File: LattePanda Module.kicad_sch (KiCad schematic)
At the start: 12 parts, among them CN78 SMTWE2055MTJ, CN79 SMTWE2055MTJ, J81 I2C

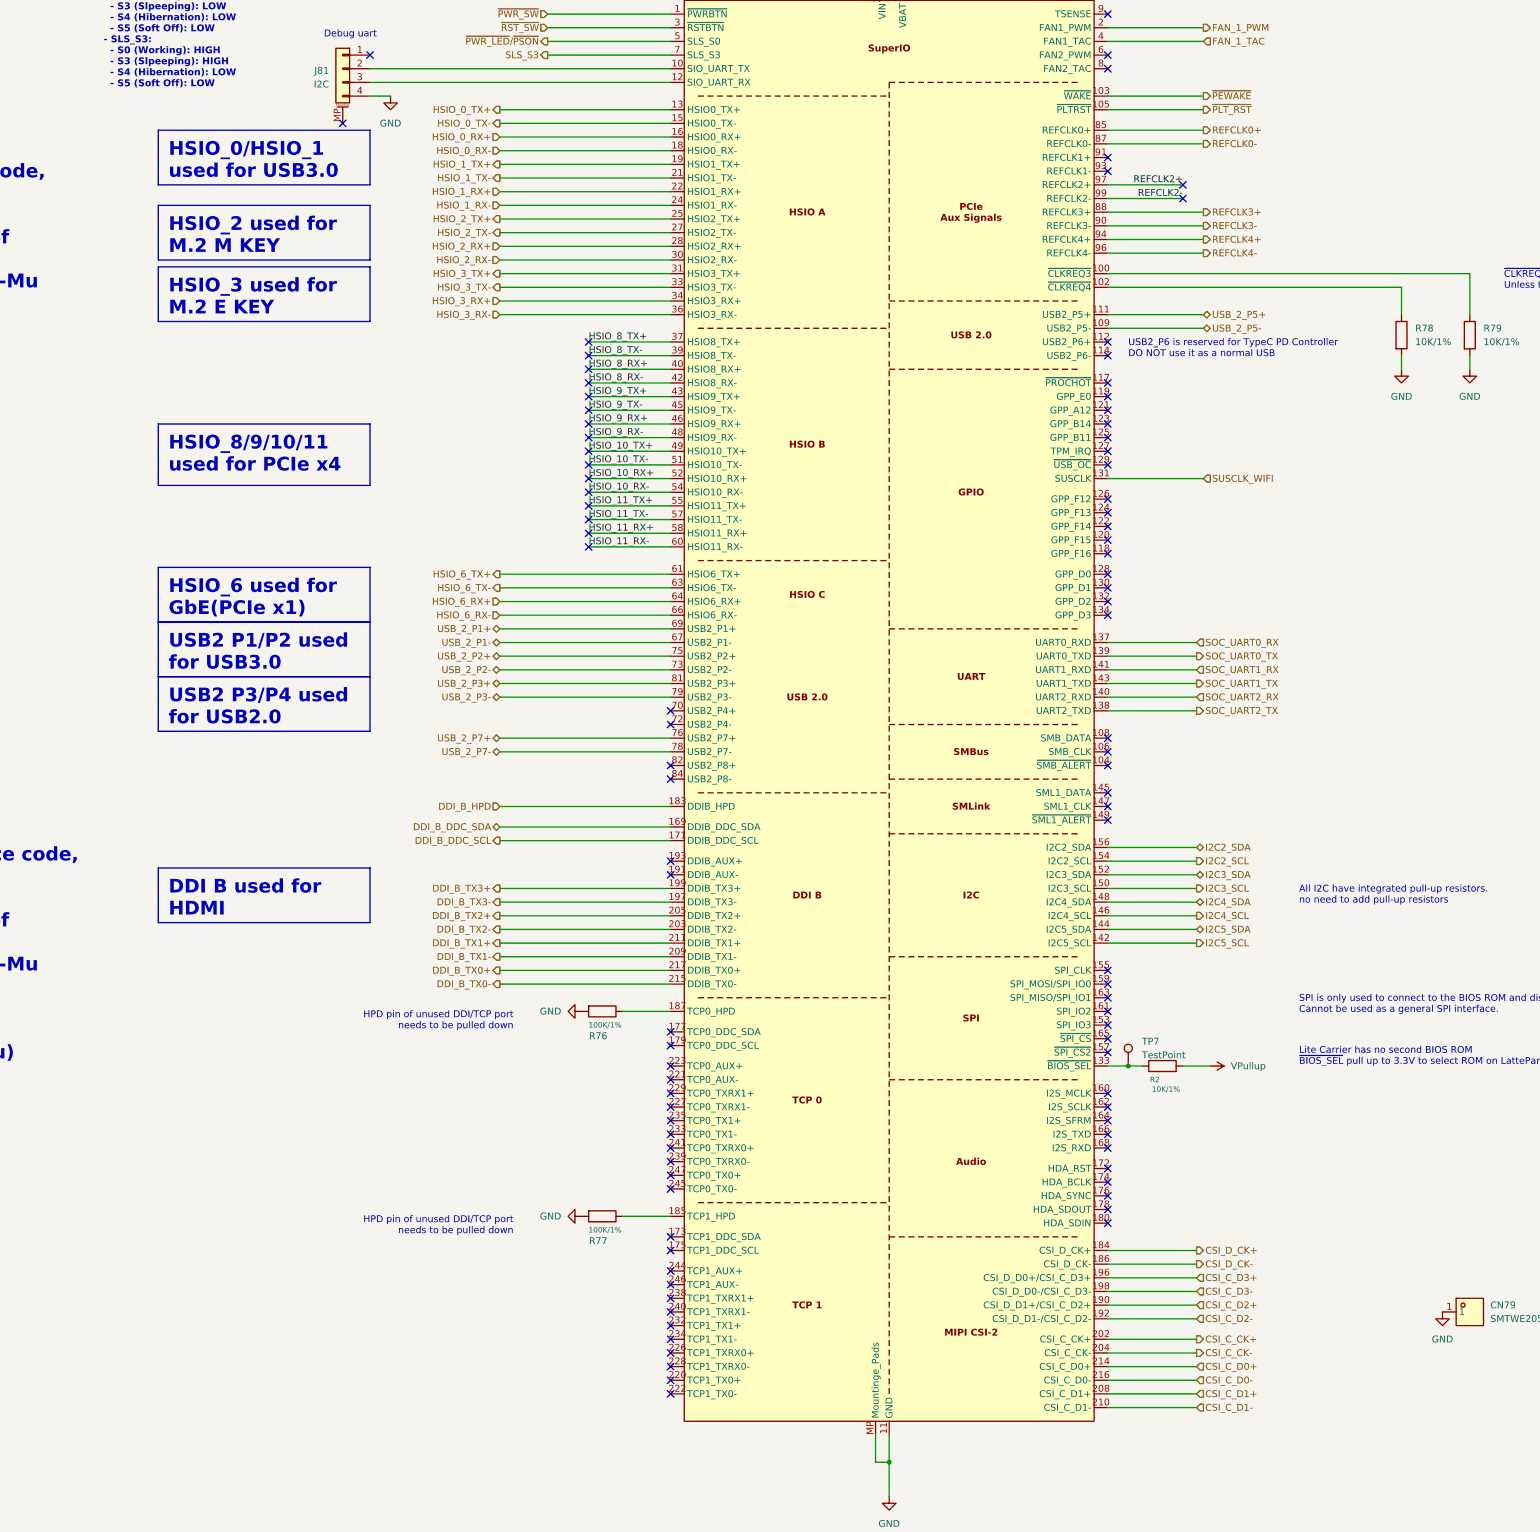
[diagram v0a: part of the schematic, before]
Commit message: hierarchical schema rework
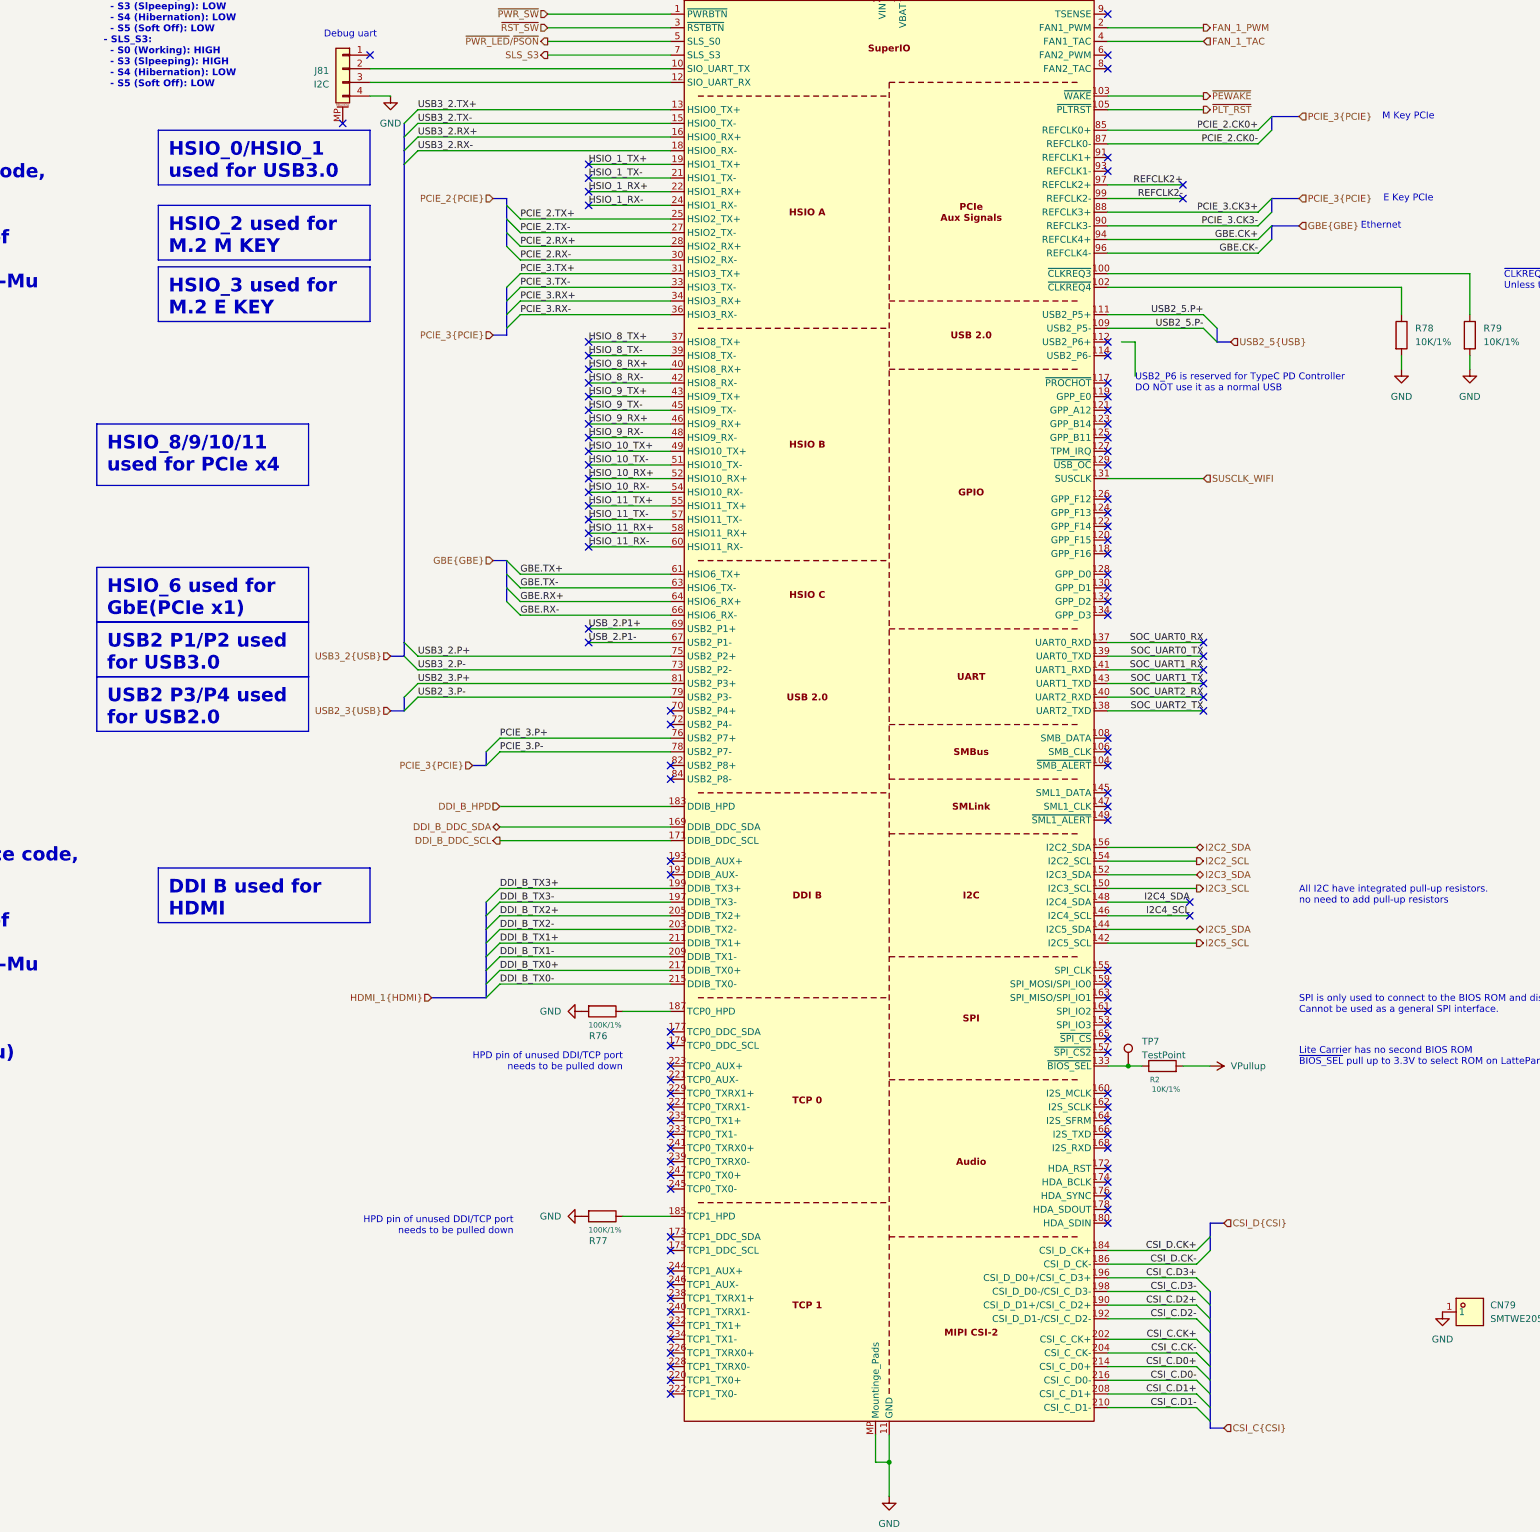
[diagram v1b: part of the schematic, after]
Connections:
- net CSI_C_CK+ renamed CSI_C.CK+
- net CSI_C_CK- renamed CSI_C.CK-
- net CSI_C_D0+ renamed CSI_C.D0+
- net CSI_C_D0- renamed CSI_C.D0-
- net CSI_C_D1+ renamed CSI_C.D1+
- net CSI_C_D1- renamed CSI_C.D1-
- net CSI_C_D2+ renamed CSI_C.D2+
- net CSI_C_D2- renamed CSI_C.D2-
- net CSI_C_D3+ renamed CSI_C.D3+
- net CSI_C_D3- renamed CSI_C.D3-
- net CSI_D_CK+ renamed CSI_D.CK+
- net CSI_D_CK- renamed CSI_D.CK-
- net HSIO_0_RX+ renamed USB3_2.RX+
- net HSIO_0_RX- renamed USB3_2.RX-
- net HSIO_0_TX+ renamed USB3_2.TX+
- net HSIO_0_TX- renamed USB3_2.TX-
- net HSIO_2_RX+ renamed PCIE_2.RX+
- net HSIO_2_RX- renamed PCIE_2.RX-
- net HSIO_2_TX+ renamed PCIE_2.TX+
- net HSIO_2_TX- renamed PCIE_2.TX-
- net HSIO_3_RX+ renamed PCIE_3.RX+
- net HSIO_3_RX- renamed PCIE_3.RX-
- net HSIO_3_TX+ renamed PCIE_3.TX+
- net HSIO_3_TX- renamed PCIE_3.TX-
- net HSIO_6_RX+ renamed GBE.RX+
- net HSIO_6_RX- renamed GBE.RX-
- net HSIO_6_TX+ renamed GBE.TX+
- net HSIO_6_TX- renamed GBE.TX-
- net REFCLK0+ renamed PCIE_2.CK0+
- net REFCLK0- renamed PCIE_2.CK0-
- net REFCLK3+ renamed PCIE_3.CK3+
- net REFCLK3- renamed PCIE_3.CK3-
- net REFCLK4+ renamed GBE.CK+
- net REFCLK4- renamed GBE.CK-
- net USB_2_P1+ renamed USB_2.P1+
- net USB_2_P1- renamed USB_2.P1-
- net USB_2_P2+ renamed USB3_2.P+
- net USB_2_P2- renamed USB3_2.P-
- net USB_2_P3+ renamed USB2_3.P+
- net USB_2_P3- renamed USB2_3.P-
- net USB_2_P5+ renamed USB2_5.P+
- net USB_2_P5- renamed USB2_5.P-
- net USB_2_P7+ renamed PCIE_3.P+
- net USB_2_P7- renamed PCIE_3.P-
- no-connect marks 96 -> 110
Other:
- note added: "E Key PCIe"
- note added: "Ethernet"
- note added: "M Key PCIe"

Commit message: prod files created
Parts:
- renumbered A1 to A78, CN79 to CN78, CN78 to CN79, J81 to J78, R1 to R78, R78 to R79, R79 to R80, R76 to R81, R2 to R82, R77 to R83, TP7 to TP78
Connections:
- net GPP_D3: now reaches A78.134 (GPP_D3)
- net DDI_B_TX0+ renamed HDMI_1.TX0+
- net DDI_B_TX0- renamed HDMI_1.TX0-
- net DDI_B_TX1+ renamed HDMI_1.TX1+
- net DDI_B_TX1- renamed HDMI_1.TX1-
- net DDI_B_TX2+ renamed HDMI_1.TX2+
- net DDI_B_TX2- renamed HDMI_1.TX2-
- net DDI_B_TX3+ renamed HDMI_1.TX3+
- net DDI_B_TX3- renamed HDMI_1.TX3-
- no-connect marks 110 -> 109
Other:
- note added: "[LATTEPANDA MU]"
